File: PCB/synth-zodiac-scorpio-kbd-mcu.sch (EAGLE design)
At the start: 58 parts, among them U1 ATmega328P-MU, U2 TL072A, X1 16MHz

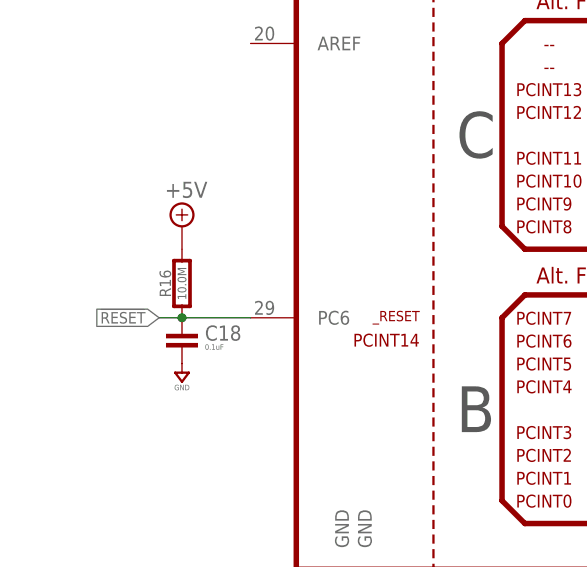
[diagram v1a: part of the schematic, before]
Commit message: Tune values and some schematic visual tweaks.
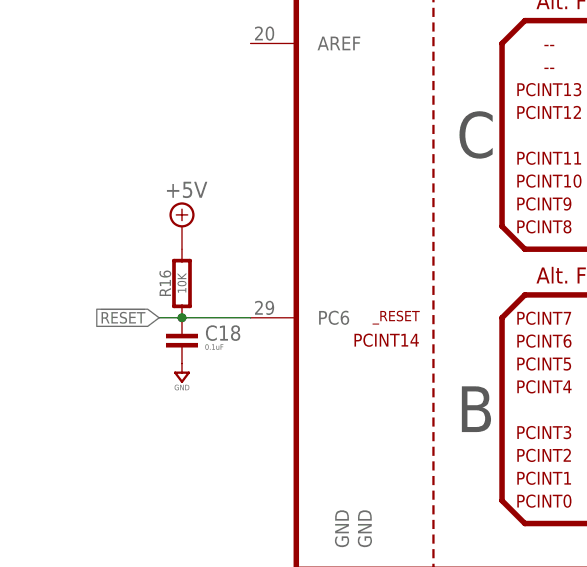
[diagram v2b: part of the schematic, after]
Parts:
- R16: value 10.0M -> 10K
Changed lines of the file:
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@@
 <part name="SUPPLY14" library="supply" library_urn="urn:adsk.eagle:library:10485988" deviceset="GND" device=""/>
 <part name="SUPPLY15" library="supply" library_urn="urn:adsk.eagle:library:10485988" deviceset="GND" device=""/>
-<part name="R16" library="rlc" library_urn="urn:adsk.eagle:library:4192893" deviceset="RESISTOR" device="0603" package3d_urn="urn:adsk.eagle:package:4193040/5" value="10.0M"/>
+<part name="R16" library="rlc" library_urn="urn:adsk.eagle:library:4192893" deviceset="RESISTOR" device="0603" package3d_urn="urn:adsk.eagle:package:4193040/5" value="10K"/>
 <part name="C18" library="rlc" library_urn="urn:adsk.eagle:library:4192893" deviceset="CAPACITOR" device="0603" package3d_urn="urn:adsk.eagle:package:4193021/5" value="0.1uF"/>
 <part name="SUPPLY16" library="supply" library_urn="urn:adsk.eagle:library:10485988" deviceset="GND" device=""/>
